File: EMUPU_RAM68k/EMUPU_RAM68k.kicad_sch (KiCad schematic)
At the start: 22 parts, among them J3 Barrel_Jack_Switch, J4 Conn_01x06_Pin, J5 Conn_01x08_Pin, SW1 SW_SPDT, SW2 SW_SPST, U1 PIC18F47Q43-IP, U2 628128, U3 68008D_AA

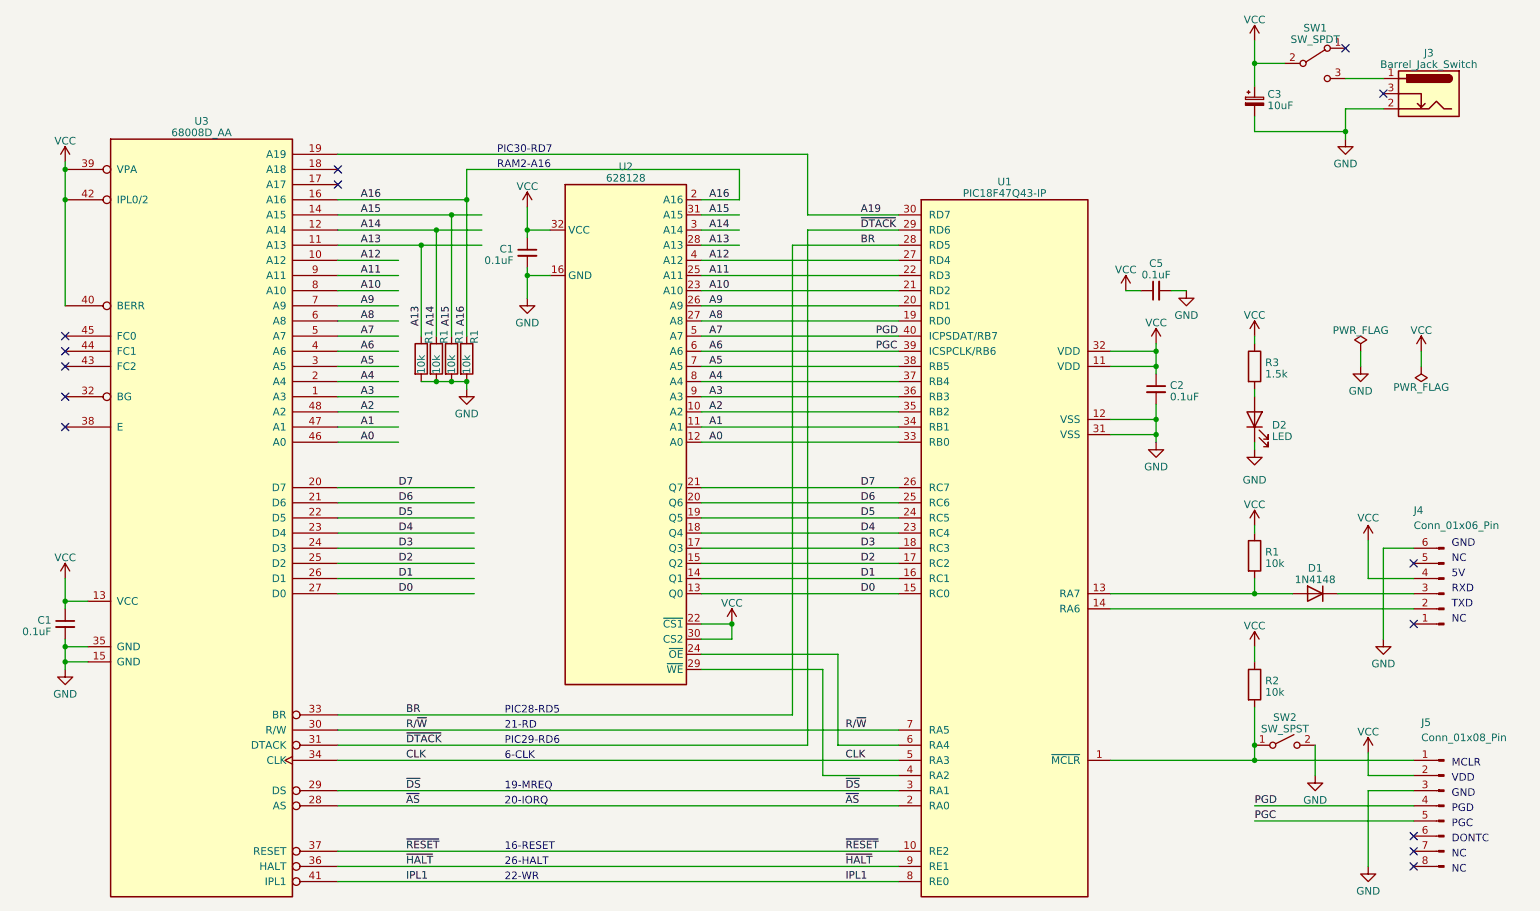
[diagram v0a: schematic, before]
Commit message: Exchange RD6 and RD7, add .gitignore
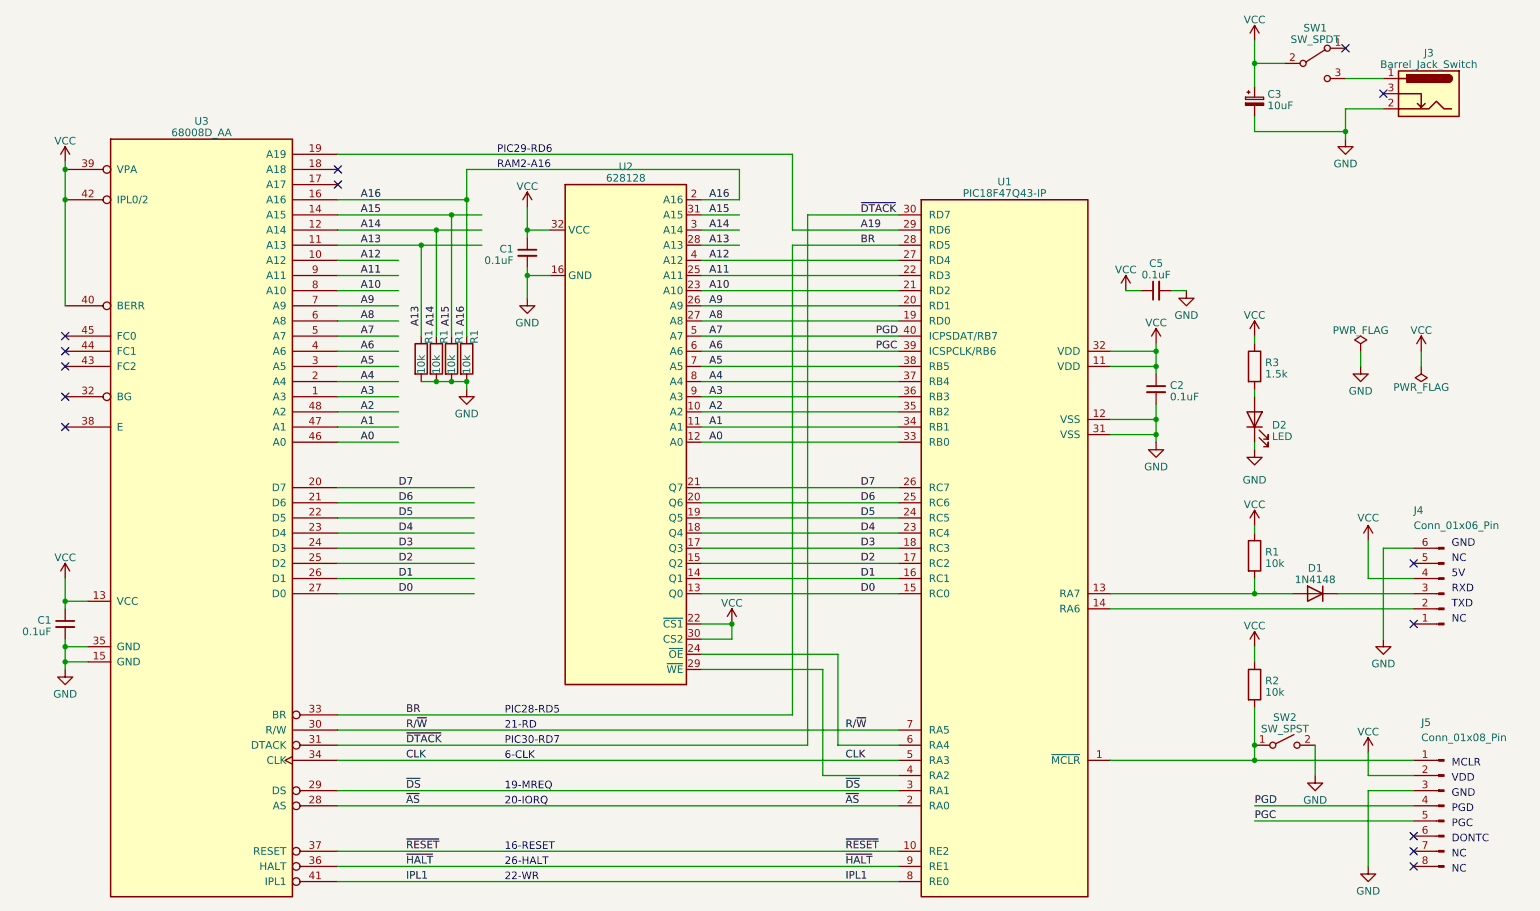
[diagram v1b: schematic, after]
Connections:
- net A19: now also U1.29 (RD6); no longer U1.30 (RD7)
- net ~{DTACK}: now also U1.30 (RD7); no longer U1.29 (RD6)
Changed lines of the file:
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@@
   (no_connect (at 40.64 71.12))
   (no_connect (at 40.64 81.28))
+  (wire (pts (xy 165.1 50.8) (xy 180.34 50.8))
+    (stroke (width 0) (type default))
+  )
   (wire (pts (xy 259.08 144.78) (xy 259.08 140.97))
     (stroke (width 0) (type default))
@@
     (stroke (width 0) (type default))
   )
-  (wire (pts (xy 86.36 40.64) (xy 165.1 40.64))
+  (wire (pts (xy 86.36 40.64) (xy 162.56 40.64))
     (stroke (width 0) (type default))
   )
@@
     (stroke (width 0) (type default))
   )
-  (wire (pts (xy 165.1 53.34) (xy 165.1 139.7))
-    (stroke (width 0) (type default))
-  )
   (wire (pts (xy 86.36 55.88) (xy 100.33 55.88))
     (stroke (width 0) (type default))
@@
     (stroke (width 0) (type default))
   )
-  (wire (pts (xy 165.1 40.64) (xy 165.1 50.8))
+  (wire (pts (xy 162.56 40.64) (xy 162.56 53.34))
     (stroke (width 0) (type default))
   )
@@
     (stroke (width 0) (type default))
   )
-  (wire (pts (xy 165.1 53.34) (xy 180.34 53.34))
-    (stroke (width 0) (type default))
-  )
   (wire (pts (xy 107.95 78.74) (xy 107.95 80.01))
     (stroke (width 0) (type default))
@@
     (stroke (width 0) (type default))
   )
-  (wire (pts (xy 165.1 50.8) (xy 180.34 50.8))
+  (wire (pts (xy 165.1 50.8) (xy 165.1 139.7))
     (stroke (width 0) (type default))
   )
@@
     (stroke (width 0) (type default))
   )
+  (wire (pts (xy 162.56 53.34) (xy 180.34 53.34))
+    (stroke (width 0) (type default))
+  )
   (wire (pts (xy 107.95 43.18) (xy 153.67 43.18))
     (stroke (width 0) (type default))
@@
     (stroke (width 0) (type default))
   )
-  (text "PIC29-RD6" (at 114.3 139.7 0)
+  (text "PIC30-RD7" (at 114.3 139.7 0)
     (effects (font (size 1.27 1.27)) (justify left bottom))
   )
@@
     (effects (font (size 1.27 1.27)) (justify left bottom))
   )
-  (text "PIC30-RD7" (at 113.03 40.64 0)
+  (text "PIC29-RD6" (at 113.03 40.64 0)
     (effects (font (size 1.27 1.27)) (justify left bottom))
   )
@@
     (effects (font (size 1.27 1.27)) (justify left bottom))
   )
-  (label "A19" (at 173.99 50.8 0) (fields_autoplaced)
+  (label "A19" (at 173.99 53.34 0) (fields_autoplaced)
     (effects (font (size 1.27 1.27)) (justify left bottom))
   )
@@
     (effects (font (size 1.27 1.27)) (justify left bottom))
   )
-  (label "~{DTACK}" (at 173.99 53.34 0) (fields_autoplaced)
-    (effects (font (size 1.27 1.27)) (justify left bottom))
-  )
+  (label "~{DTACK}" (at 173.99 50.8 0) (fields_autoplaced)
+    (effects (font (size 1.27 1.27)) (justify left bottom))
+  )

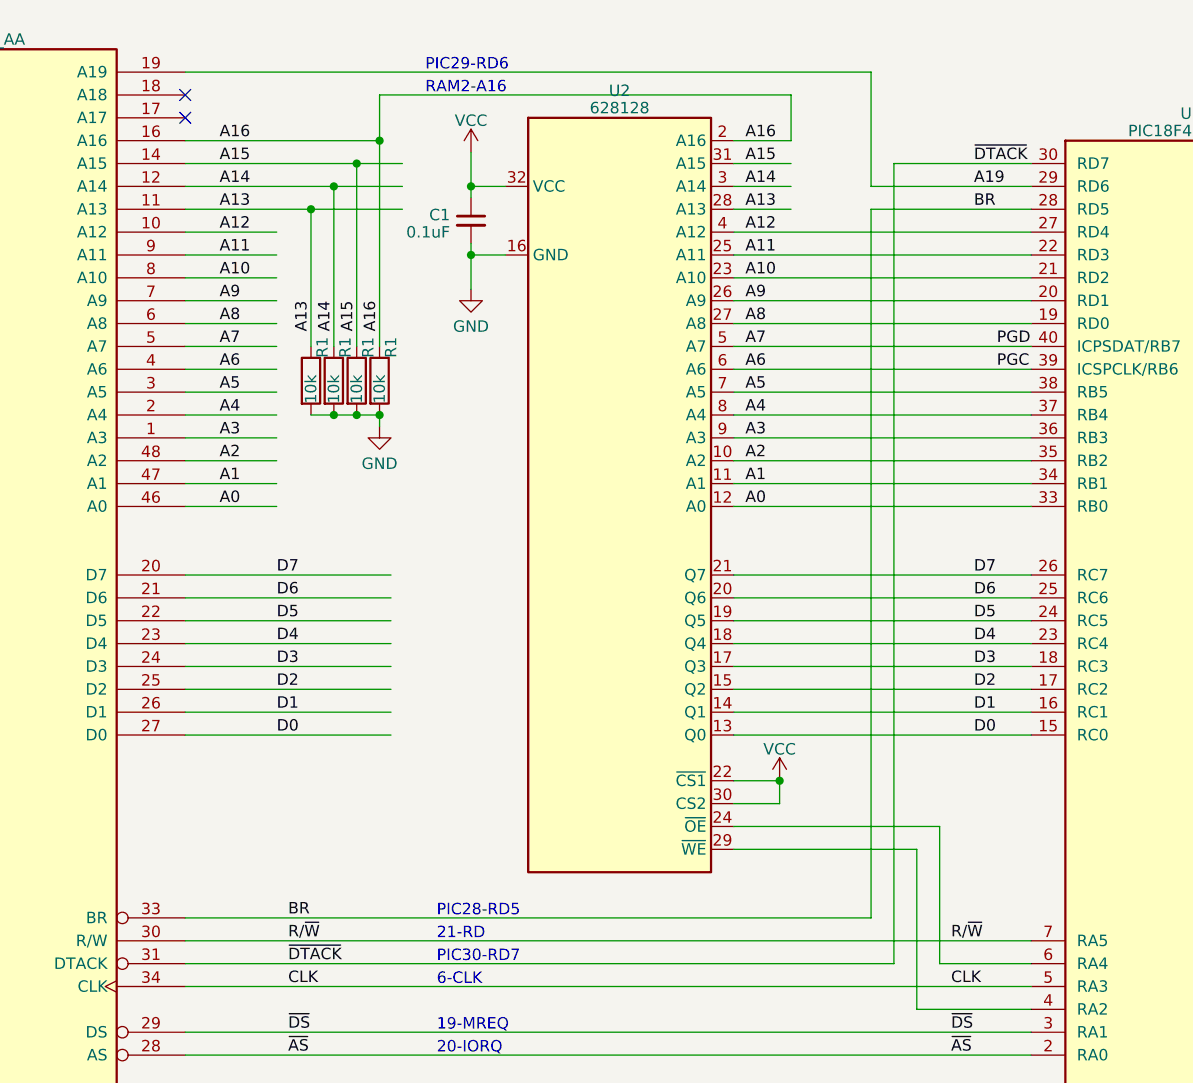
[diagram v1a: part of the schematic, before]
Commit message: Cut BR-PIC RD5, and add TEST pin
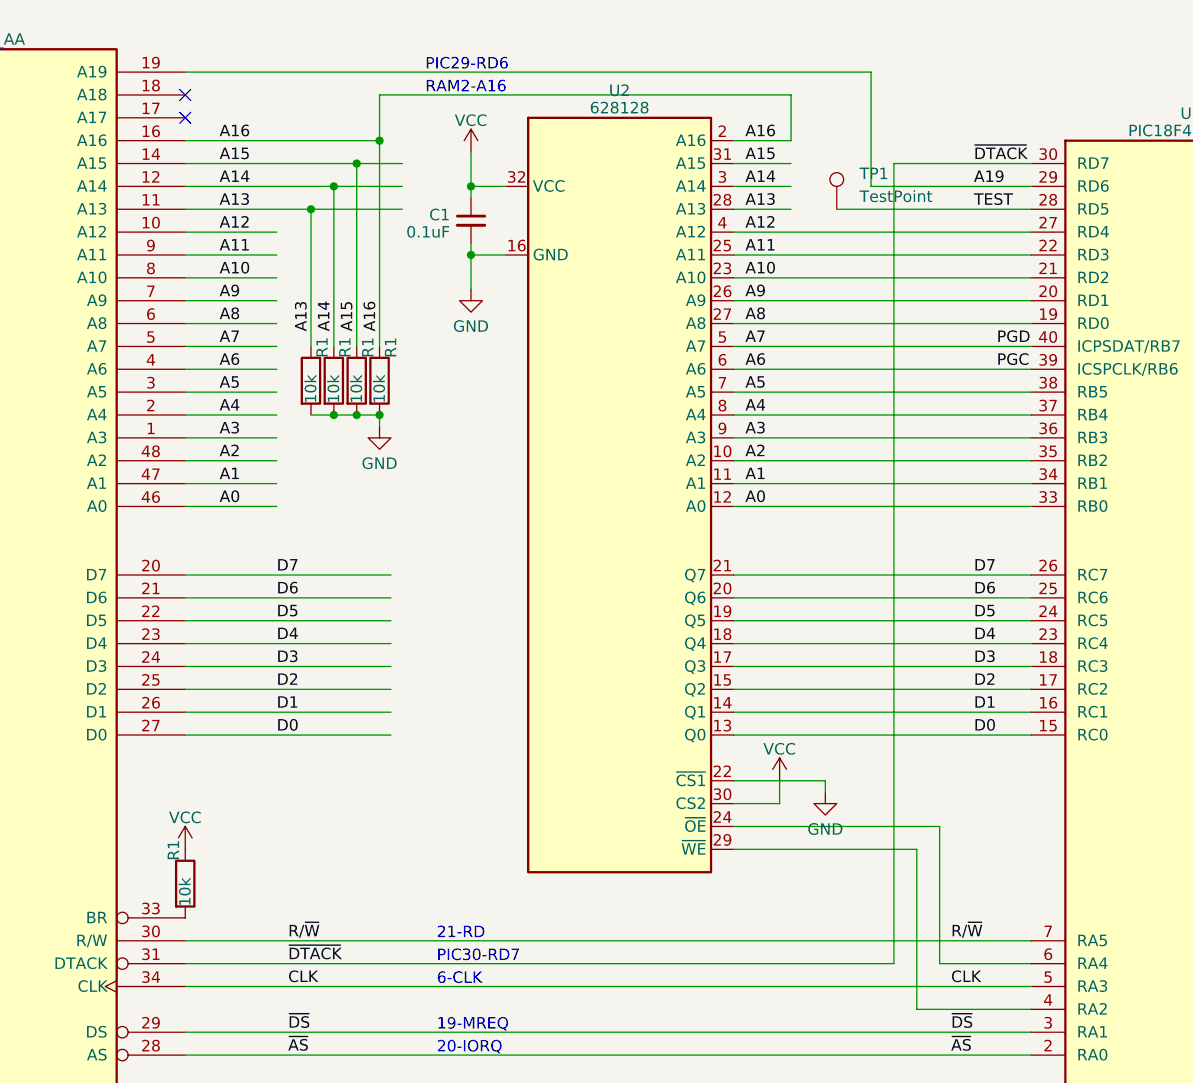
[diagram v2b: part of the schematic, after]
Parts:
- added R1: 10k, Resistor_THT:R_Axial_DIN0204_L3.6mm_D1.6mm_P7.62mm_Horizontal, symbol Device:R
- added TP1: TestPoint, symbol Connector:TestPoint
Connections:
- net GND: now also U2.22 (~{CS1})
- net VCC: now also R1.1; no longer U2.22 (~{CS1})
- net BR: no longer names the net of U3.33 (BR)
- net BR: now also R1.2; no longer U1.28 (RD5)
- new net TEST: TP1.1, U1.28 (RD5)
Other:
- note removed: "PIC28-RD5"
- title: (none) -> EMUPU_RAM 68k8 Version
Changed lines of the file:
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@@
 (kicad_sch (version 20230121) (generator eeschema)
   (paper "A4")
+  (title_block
+    (title "EMUPU_RAM 68k8 Version")
+    (rev "Rev. 003")
+  )
   (junction (at 223.52 87.63) (diameter 0) (color 0 0 0 0)
   )
@@
   )
   (junction (at 102.87 53.34) (diameter 0) (color 0 0 0 0)
-  )
-  (junction (at 152.4 119.38) (diameter 0) (color 0 0 0 0)
   )
   (junction (at 102.87 78.74) (diameter 0) (color 0 0 0 0)
@@
     (stroke (width 0) (type default))
   )
-  (wire (pts (xy 180.34 55.88) (xy 162.56 55.88))
+  (wire (pts (xy 180.34 55.88) (xy 158.75 55.88))
     (stroke (width 0) (type default))
   )
@@
     (stroke (width 0) (type default))
   )
-  (wire (pts (xy 86.36 134.62) (xy 162.56 134.62))
-    (stroke (width 0) (type default))
-  )
   (wire (pts (xy 102.87 78.74) (xy 105.41 78.74))
     (stroke (width 0) (type default))
@@
     (stroke (width 0) (type default))
   )
-  (wire (pts (xy 162.56 55.88) (xy 162.56 134.62))
-    (stroke (width 0) (type default))
-  )
   (wire (pts (xy 223.52 82.55) (xy 223.52 85.09))
     (stroke (width 0) (type default))
@@
     (stroke (width 0) (type default))
   )
-  (wire (pts (xy 147.32 119.38) (xy 152.4 119.38))
+  (wire (pts (xy 147.32 119.38) (xy 157.48 119.38))
     (stroke (width 0) (type default))
   )
@@
     (stroke (width 0) (type default))
   )
+  (wire (pts (xy 157.48 119.38) (xy 157.48 120.65))
+    (stroke (width 0) (type default))
+  )
   (wire (pts (xy 147.32 114.3) (xy 180.34 114.3))
     (stroke (width 0) (type default))
@@
   )
   (text "MCLR" (at 273.05 143.51 0)
-    (effects (font (size 1.27 1.27)) (justify left bottom))
-  )
-  (text "PIC28-RD5" (at 114.3 134.62 0)
     (effects (font (size 1.27 1.27)) (justify left bottom))
   )
@@
     (effects (font (size 1.27 1.27)) (justify left bottom))
   )
-  (label "BR" (at 97.79 134.62 0) (fields_autoplaced)
-    (effects (font (size 1.27 1.27)) (justify left bottom))
-  )
   (label "A8" (at 148.59 68.58 0) (fields_autoplaced)
     (effects (font (size 1.27 1.27)) (justify left bottom))
@@
     (effects (font (size 1.27 1.27)) (justify left bottom))
   )
-  (label "BR" (at 173.99 55.88 0) (fields_autoplaced)
+  (label "TEST" (at 173.99 55.88 0) (fields_autoplaced)
     (effects (font (size 1.27 1.27)) (justify left bottom))
   )
@@
     )
   )
+  (symbol (lib_id "Device:R") (at 86.36 130.81 0) (unit 1)
+    (in_bom yes) (on_board yes) (dnp no)
+    (property "Reference" "R1" (at 85.09 128.27 90)
+      (effects (font (size 1.27 1.27)) (justify left))
+    )
+    (property "Value" "10k" (at 86.36 133.35 90)
+      (effects (font (size 1.27 1.27)) (justify left))
+    )
+    (property "Footprint" "Resistor_THT:R_Axial_DIN0204_L3.6mm_D1.6mm_P7.62mm_Horizontal" (at 84.582 130.81 90)
+      (effects (font (size 1.27 1.27)) hide)
+    )
+    (property "Datasheet" "~" (at 86.36 130.81 0)
+      (effects (font (size 1.27 1.27)) hide)
+    )
+    (pin "1")
+    (pin "2")
+    (instances
+      (project "EMUPU_RAM"
+        (path "/6d2188b2-a6ec-4341-9e2f-19ddbe5554d2"
+          (reference "R1") (unit 1)
+        )
+      )
+      (project "EMUPU_RAM68k"
+        (path "/e6d6b00c-3eac-46b2-864a-d30920c7bbcf"
+          (reference "R8") (unit 1)
+        )
+      )
+    )
+  )
   (symbol (lib_id "power:VCC") (at 267.97 73.66 0) (unit 1)
     (in_bom yes) (on_board yes) (dnp no) (fields_autoplaced)
@@
     )
   )
+  (symbol (lib_id "power:GND") (at 157.48 120.65 0) (unit 1)
+    (in_bom yes) (on_board yes) (dnp no) (fields_autoplaced)
+    (property "Reference" "#PWR08" (at 157.48 127 0)
+      (effects (font (size 1.27 1.27)) hide)
+    )
+    (property "Value" "GND" (at 157.48 124.7855 0)
+      (effects (font (size 1.27 1.27)))
+    )
+    (property "Footprint" "" (at 157.48 120.65 0)
+      (effects (font (size 1.27 1.27)) hide)
+    )
+    (property "Datasheet" "" (at 157.48 120.65 0)
+      (effects (font (size 1.27 1.27)) hide)
+    )
+    (pin "1")
+    (instances
+      (project "EMUPU_RAM"
+        (path "/6d2188b2-a6ec-4341-9e2f-19ddbe5554d2"
+          (reference "#PWR08") (unit 1)
+        )
+      )
+      (project "EMUPU_RAM68k"
+        (path "/e6d6b00c-3eac-46b2-864a-d30920c7bbcf"
+          (reference "#PWR025") (unit 1)
+        )
+      )
+    )
+  )
   (symbol (lib_id "power:VCC") (at 259.08 140.97 0) (unit 1)
     (in_bom yes) (on_board yes) (dnp no) (fields_autoplaced)
@@
         (path "/e6d6b00c-3eac-46b2-864a-d30920c7bbcf"
           (reference "#PWR08") (unit 1)
+        )
+      )
+    )
+  )
+  (symbol (lib_id "Connector:TestPoint") (at 158.75 55.88 0) (unit 1)
+    (in_bom yes) (on_board yes) (dnp no) (fields_autoplaced)
+    (property "Reference" "TP1" (at 161.29 51.943 0)
+      (effects (font (size 1.27 1.27)) (justify left))
+    )
+    (property "Value" "TestPoint" (at 161.29 54.483 0)
+      (effects (font (size 1.27 1.27)) (justify left))
+    )
+    (property "Footprint" "" (at 163.83 55.88 0)
+      (effects (font (size 1.27 1.27)) hide)
+    )
+    (property "Datasheet" "~" (at 163.83 55.88 0)
+      (effects (font (size 1.27 1.27)) hide)
+    )
+    (pin "1")
+    (instances
+      (project "EMUPU_RAM68k"
+        (path "/e6d6b00c-3eac-46b2-864a-d30920c7bbcf"
+          (reference "TP1") (unit 1)
         )
       )
@@
         )
       )
+    )
+  )
+  (symbol (lib_id "power:VCC") (at 86.36 127 0) (unit 1)
+    (in_bom yes) (on_board yes) (dnp no) (fields_autoplaced)
+    (property "Reference" "#PWR02" (at 86.36 130.81 0)
+      (effects (font (size 1.27 1.27)) hide)
+    )
+    (property "Value" "VCC" (at 86.36 123.4981 0)
+      (effects (font (size 1.27 1.27)))
+    )
+    (property "Footprint" "" (at 86.36 127 0)
+      (effects (font (size 1.27 1.27)) hide)
+    )
+    (property "Datasheet" "" (at 86.36 127 0)
+      (effects (font (size 1.27 1.27)) hide)
+    )
+    (pin "1")
+    (instances
+      (project "EMUPU_RAM"
+        (path "/6d2188b2-a6ec-4341-9e2f-19ddbe5554d2"
+          (reference "#PWR02") (unit 1)
+        )
+      )
+      (project "EMUPU_RAM68k"
+        (path "/e6d6b00c-3eac-46b2-864a-d30920c7bbcf"
+          (reference "#PWR024") (unit 1)
+        )
+      )
